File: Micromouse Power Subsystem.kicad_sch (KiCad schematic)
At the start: 3 parts, among them J2 Conn_02x16_Odd_Even, U1 INA219AxD

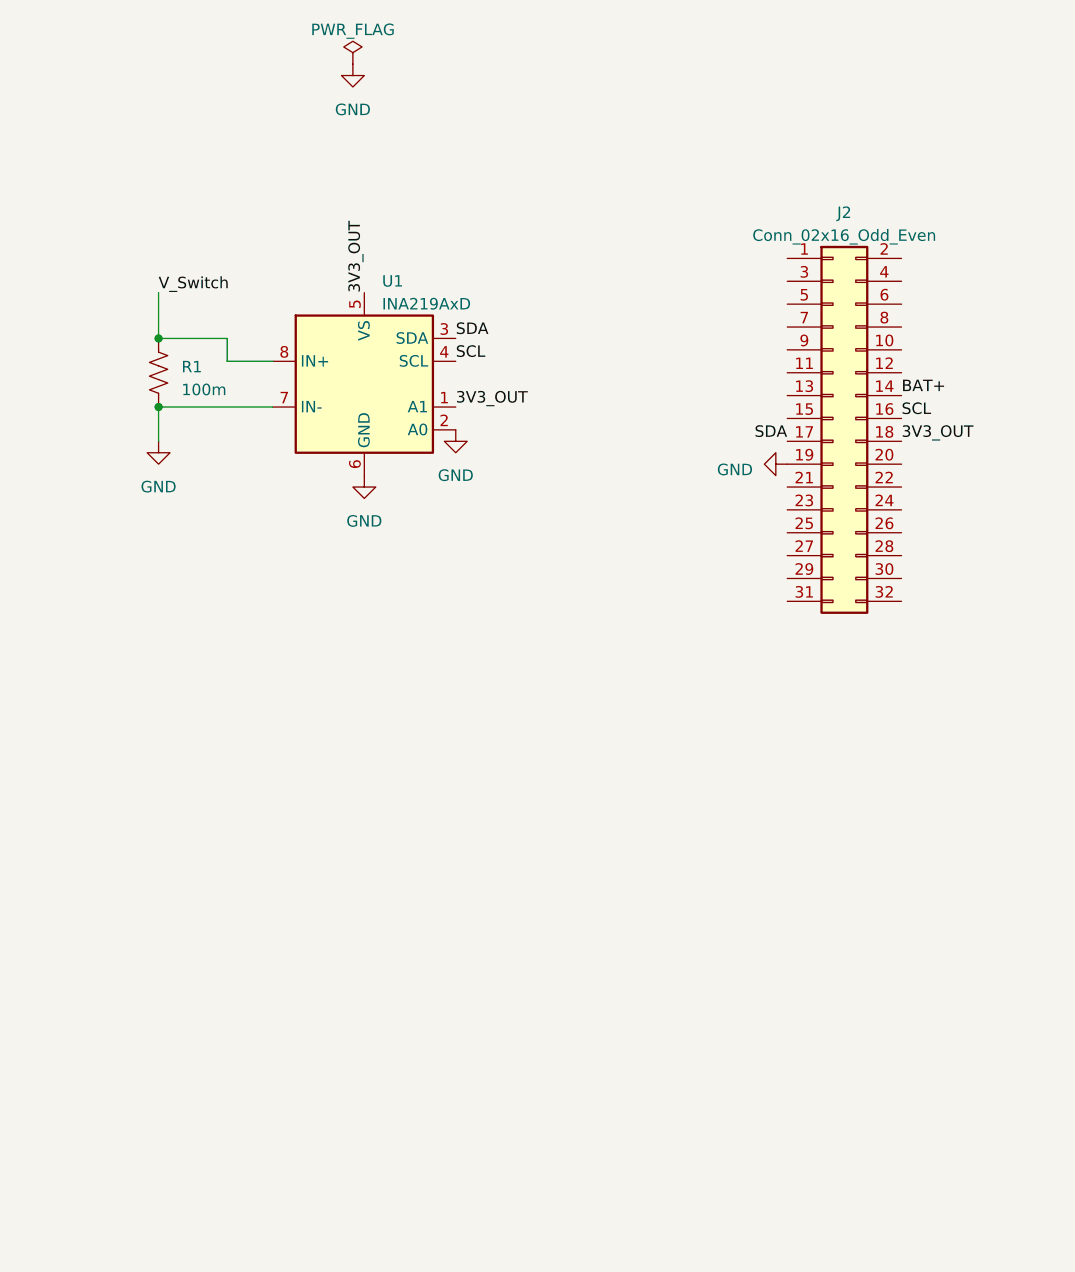
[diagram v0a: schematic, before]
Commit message: Kiyuran Task 1 Schematic Implementation Done: Added 2x external load switches with SI2301 (P-MOSFET) and 2N3904 (NPN Transistor)
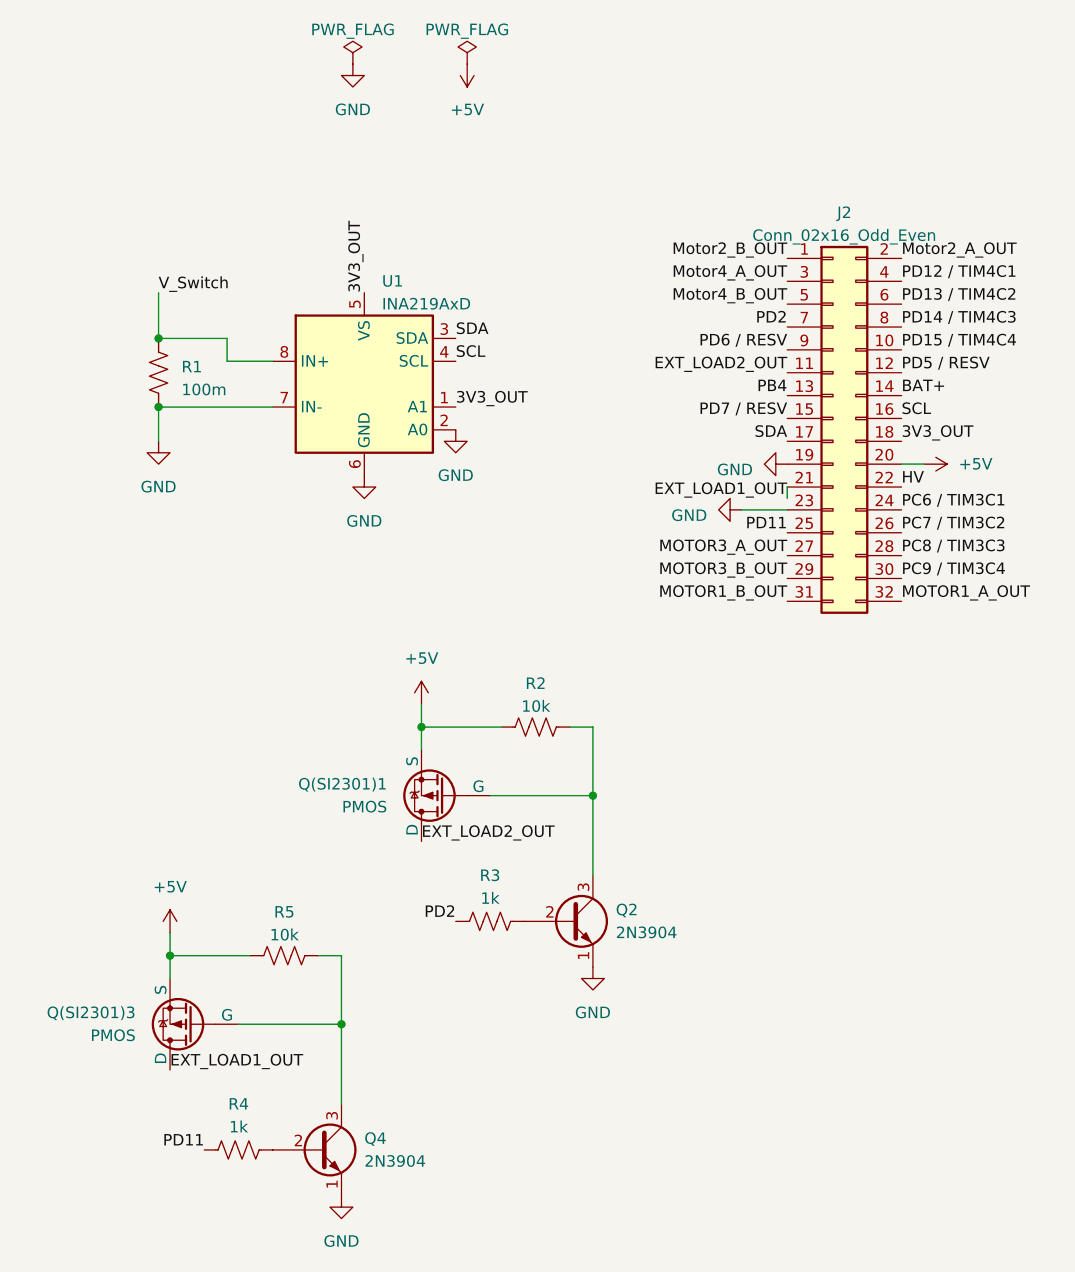
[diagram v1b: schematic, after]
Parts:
- added Q(SI2301)1, Q(SI2301)3: PMOS, symbol Simulation_SPICE:PMOS
- added Q2, Q4: 2N3904, Package_TO_SOT_THT:TO-92_Inline, symbol Transistor_BJT:2N3904
- added R2, R5: 10k, symbol Device:R_US
- added R3, R4: 1k, symbol Device:R_US
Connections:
- net GND: now also J2.23 (Pin_23), Q2.1 (E), Q4.1 (E)
- net Motor2_B_OUT: now reaches J2.1 (Pin_1)
- net PD15 / TIM4C4: now reaches J2.10 (Pin_10)
- net EXT_LOAD2_OUT: now reaches J2.11 (Pin_11)
- net EXT_LOAD2_OUT: now also Q(SI2301)1.1 (D)
- net PD5 / RESV: now reaches J2.12 (Pin_12)
- net PB4: now reaches J2.13 (Pin_13)
- net PD7 / RESV: now reaches J2.15 (Pin_15)
- net Motor2_A_OUT: now reaches J2.2 (Pin_2)
- net +5V: now reaches J2.20 (Pin_20)
- net +5V: now also Q(SI2301)1.3 (S), Q(SI2301)3.3 (S), R2.1, R5.1
- net EXT_LOAD1_OUT: now reaches J2.21 (Pin_21)
- net EXT_LOAD1_OUT: now also Q(SI2301)3.1 (D)
- net HV: now reaches J2.22 (Pin_22)
- net PC6 / TIM3C1: now reaches J2.24 (Pin_24)
- net PD11: now reaches J2.25 (Pin_25)
- net PD11: now also R4.1
- net PC7 / TIM3C2: now reaches J2.26 (Pin_26)
- net MOTOR3_A_OUT: now reaches J2.27 (Pin_27)
- net PC8 / TIM3C3: now reaches J2.28 (Pin_28)
- net MOTOR3_B_OUT: now reaches J2.29 (Pin_29)
- net Motor4_A_OUT: now reaches J2.3 (Pin_3)
- net PC9 / TIM3C4: now reaches J2.30 (Pin_30)
- net MOTOR1_B_OUT: now reaches J2.31 (Pin_31)
- net MOTOR1_A_OUT: now reaches J2.32 (Pin_32)
- net PD12 / TIM4C1: now reaches J2.4 (Pin_4)
- net Motor4_B_OUT: now reaches J2.5 (Pin_5)
- net PD13 / TIM4C2: now reaches J2.6 (Pin_6)
- net PD2: now reaches J2.7 (Pin_7)
- net PD2: now also R3.1
- net PD14 / TIM4C3: now reaches J2.8 (Pin_8)
- net PD6 / RESV: now reaches J2.9 (Pin_9)
- new net: Q2.2 (B), R3.2
- new net: Q(SI2301)1.2 (G), Q2.3 (C), R2.2
- new net: Q(SI2301)3.2 (G), Q4.3 (C), R5.2
- new net: Q4.2 (B), R4.2

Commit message: (K.2:) Added and updated Task 2: Added generic JST PH (Conn_01x02) for BAT+ to VM1/VM2/VM3 and GND to PGND2/PGND1/GND on both TB6612FNG's with 100uF and 0.1uF caps
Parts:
- removed Q(SI2301)3: PMOS, symbol Simulation_SPICE:PMOS
- removed Q4: 2N3904, Package_TO_SOT_THT:TO-92_Inline, symbol Transistor_BJT:2N3904
- added C1: 100µ, symbol Device:C_Small
- added C2: 0.1µ, symbol Device:C_Small
- added J1: Conn_01x02, Connector_JST:JST_PH_B2B-PH-K_1x02_P2.00mm_Vertical, symbol Connector_Generic:Conn_01x02
- added Q(SI2301)2: PMOS, symbol Simulation_SPICE:PMOS
- added Q1: 2N3904, Package_TO_SOT_THT:TO-92_Inline, symbol Transistor_BJT:2N3904
- added U2, U3: TB6612FNG, Package_SO:SSOP-24_5.3x8.2mm_P0.65mm, symbol Driver_Motor:TB6612FNG
- R1: footprint (none) -> Resistor_SMD:R_Shunt_Ohmite_LVK12
- R2: value 10k -> 1k
- R3: value 1k -> 10k
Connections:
- net 3V3_OUT: now also U2.19 (STBY), U2.20 (VCC), U3.19 (STBY), U3.20 (VCC)
- net BAT+: now also C1.1, C2.1, J1.1 (Pin_1), U2.13 (VM2), U2.14 (VM3), U2.24 (VM1), U3.13 (VM2), U3.14 (VM3), U3.24 (VM1)
- net EXT_LOAD1_OUT: now also Q(SI2301)1.1 (D)
- net EXT_LOAD2_OUT: now also Q(SI2301)2.1 (D); no longer Q(SI2301)1.1 (D)
- net GND: now also C1.2, C2.2, J1.2 (Pin_2), Q1.1 (E), U2.10 (PGND2), U2.18 (GND), U2.3 (PGND1), U2.4 (PGND1), U2.9 (PGND2), U3.10 (PGND2), U3.18 (GND), U3.3 (PGND1), U3.4 (PGND1), U3.9 (PGND2)
- net Motor2_A_OUT: now also U2.1 (AO1), U2.2 (AO1)
- net Motor2_B_OUT: now also U2.5 (AO2), U2.6 (AO2)
- net Motor4_A_OUT: now also U2.11 (BO1), U2.12 (BO1)
- net Motor4_B_OUT: now also U2.7 (BO2), U2.8 (BO2)
- net at R3.2: now also Q(SI2301)1.2 (G), Q1.3 (C); no longer Q2.2 (B)
- net at R5.2: now also Q2.3 (C), Q(SI2301)2.2 (G)
- net at R4.2: now also Q2.2 (B)
- net +5V renamed 5V_OUT
- net 5V_OUT: now also R3.1, Q(SI2301)2.3 (S); no longer R2.1
- net MOTOR1_A_OUT renamed Motor1_A_OUT
- net Motor1_A_OUT: now also U3.11 (BO1), U3.12 (BO1)
- net MOTOR1_B_OUT renamed Motor1_B_OUT
- net Motor1_B_OUT: now also U3.7 (BO2), U3.8 (BO2)
- net MOTOR3_A_OUT renamed Motor3_A_OUT
- net Motor3_A_OUT: now also U3.1 (AO1), U3.2 (AO1)
- net MOTOR3_B_OUT renamed Motor3_B_OUT
- net Motor3_B_OUT: now also U3.5 (AO2), U3.6 (AO2)
- net PB4 renamed FAST_CHARGE_CTRL
- net PC6 / TIM3C1 renamed Motor3_CTRL1
- net Motor3_CTRL1: now also U3.23 (PWMA)
- net PC7 / TIM3C2 renamed Motor3_CTRL2
- net Motor3_CTRL2: now also U3.21 (AIN1), U3.22 (AIN2)
- net PC8 / TIM3C3 renamed MotorR1_CTRL1
- net PC9 / TIM3C4 renamed Motor1_CTRL2
- net Motor1_CTRL2: now also U3.16 (BIN2), U3.17 (BIN1)
- net PD11 renamed CTRL_EXT_LOAD1
- net CTRL_EXT_LOAD1: now also R2.1; no longer R4.1
- net PD12 / TIM4C1 renamed Motor2_CTRL1
- net Motor2_CTRL1: now also U2.23 (PWMA)
- net PD13 / TIM4C2 renamed Motor2_CTRL2
- net Motor2_CTRL2: now also U2.21 (AIN1), U2.22 (AIN2)
- net PD14 / TIM4C3 renamed Motor4_CTRL1
- net Motor4_CTRL1: now also U2.15 (PWMB)
- net PD15 / TIM4C4 renamed Motor4_CTRL2
- net Motor4_CTRL2: now also U2.16 (BIN2), U2.17 (BIN1)
- net PD2 renamed CTRL_EXT_LOAD2
- net CTRL_EXT_LOAD2: now also R4.1; no longer R3.1
- net PD5 / RESV renamed USART2_TX
- net PD6 / RESV renamed USART2_RX
- net PD7 / RESV: no longer names the net of J2.15 (Pin_15)
- new net: Q1.2 (B), R2.2
- new net Motor1_CTRL1: U3.15 (PWMB)
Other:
- note added: "(K:) Provide 2x External Load Switching at 1A each (High Side connected to 5V)"
- moved on the sheet: J2, R1, U1

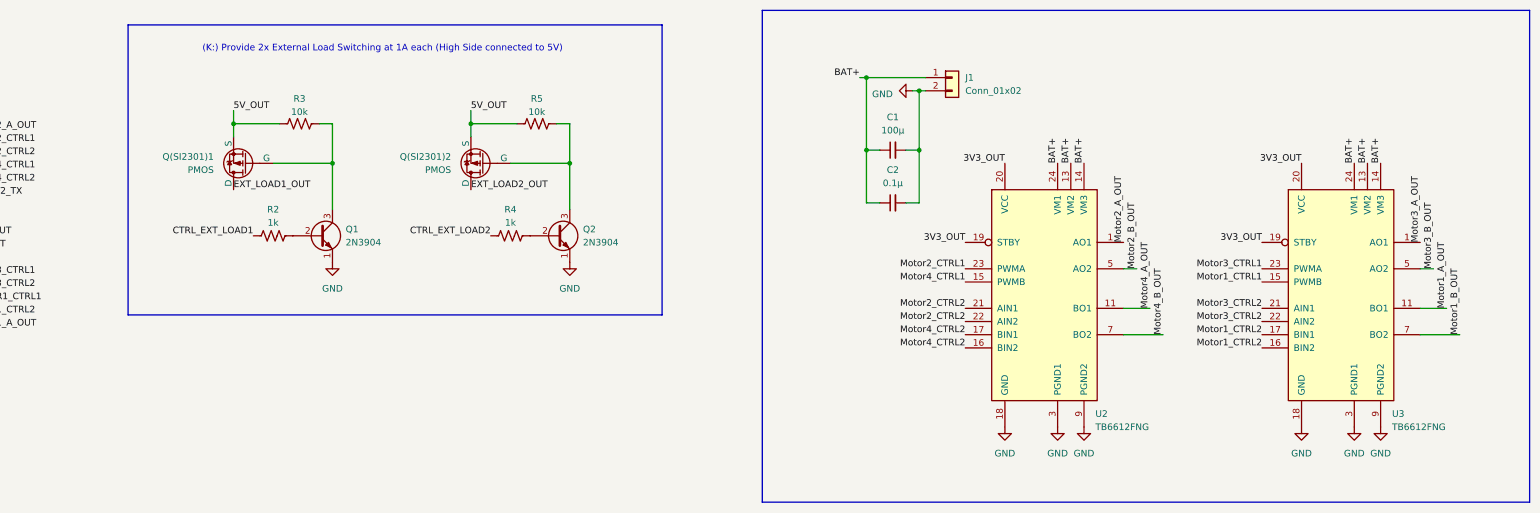
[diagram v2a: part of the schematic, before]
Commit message: (K.2:) Task 2: Used JST1/JST2 net labels at BAT+ and GND on pin 1 and 2 of J1 for clarity and to distinguish from the 2x16 header connections
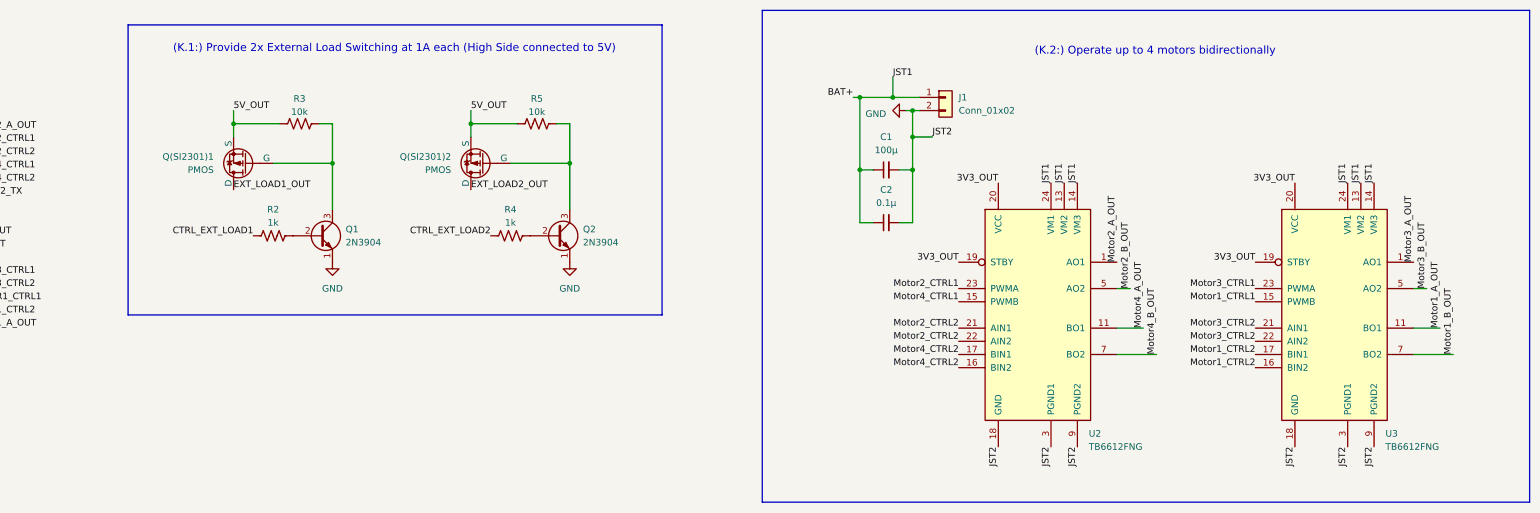
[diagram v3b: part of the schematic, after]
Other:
- note added: "(K.1:) Provide 2x External Load Switching at 1A each (High Side connected to 5V)"
- note added: "(K.2:) Operate up to 4 motors bidirectionally"
- note removed: "(K:) Provide 2x External Load Switching at 1A each (High Side connected to 5V)"
- moved on the sheet: C1, C2, J1, U2, U3

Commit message: (K.3:) Task 3: TPS61088RHLR (5V boost) and RT8059GJ5 (3.3V buck) connected with full pinout to satisfy the specifications
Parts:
- added C10, C5, C6: 10µ, symbol Device:C_Small
- added C3, C4, C9: 22µ, symbol Device:C_Small
- added C7: 1µ, symbol Device:C_Small
- added C8: 0.1µ, symbol Device:C_Small
- added L1: 2.2µ, symbol Device:L
- added L2: 4.7µ, symbol Device:L
- added Q(SI2301)3: PMOS, symbol Simulation_SPICE:PMOS
- added Q3: 2N7002, Package_TO_SOT_SMD:SOT-23, symbol Transistor_FET:2N7002
- added R10: 510k, Resistor_SMD:R_Shunt_Ohmite_LVK12, symbol Device:R_US
- added R11, R12, R6, R8: 100k, Resistor_SMD:R_Shunt_Ohmite_LVK12, symbol Device:R_US
- added R13: 10k, Resistor_SMD:R_Shunt_Ohmite_LVK12, symbol Device:R_US
- added R14: 1M, Resistor_SMD:R_Shunt_Ohmite_LVK12, symbol Device:R_US
- added R7: 19k, Resistor_SMD:R_Shunt_Ohmite_LVK12, symbol Device:R_US
- added R9: 22k, Resistor_SMD:R_Shunt_Ohmite_LVK12, symbol Device:R_US
- added SW1: ~, TS-1101S-C-B-B-B-A:SW-SMD_L6.0-W3.5-LS8.0, symbol TS-1101S-C-B-B-B-A:TS-1101S-C-B-B-B-A
- added U4: SI2301CDS-T1-GE3, TO-236_VIS, symbol 2025-03-26_09-12-34:SI2301CDS-T1-GE3
- added U5: TPS61088RHLR, TPS61088RHLR:IC_TPS61088RHLR, symbol TPS61088RHLR:TPS61088RHLR
- added U6: RT8059GJ5, TSOT-23-5_RIT, symbol 2025-03-25_16-49-52:RT8059GJ5
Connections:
- net 3V3_OUT: now also C10.2, C3.1, C5.1, C6.1, C9.2, L2.2, Q(SI2301)3.1 (D), R8.1, U5.2 (EN), U5.9 (VIN), U6.4 (VIN)
- net 5V_OUT: now also C4.1, L1.1, R6.2, U5.14 (VOUT_16), U5.15 (VOUT_14), U5.16 (VOUT_15)
- net BAT+: now also Q(SI2301)3.3 (S), R14.1, U6.1 (EN)
- net GND: now also C10.1, C3.2, C4.2, C5.2, C6.2, C7.2, C9.1, Q3.2 (S), R11.1, R12.2, R7.2, R9.1, U5.11 (NC_11), U5.12 (NC_12), U5.20 (AGND), U5.21 (PGND), U5.22 (PGND), U5.23 (PGND), U5.24 (PGND), U5.25 (PGND), U5.26 (PGND), U5.27 (PGND), U5.28 (PGND), U5.29 (PGND), U6.2 (GND)
- new net: Q(SI2301)3.2 (G), Q3.3 (D), R13.2
- new net: C7.1, U5.1 (VCC)
- new net: Q3.1 (G), R12.1, SW1.2
- new net: R6.1, R7.1, U5.17 (FB)
- new net: R14.2, SW1.1
- new net: R10.1, U5.3 (FSW)
- new net: R8.2, R9.2, U6.5 (FB)
- new net: C8.1, U5.8 (BOOT)
- new net: R11.2, U5.19 (ILIM)
- new net: L2.1, U6.3 (LLX)
- new net SW: C8.2, L1.2, R10.2, U5.4 (SW_7), U5.5 (SW_4), U5.6 (SW_5), U5.7 (SW_6)
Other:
- note added: "(K.3:) Provide an ON/OFF switch. OFF state: battery draw <30uA. ON state: can provide your robot peak current of 2A. The switch needs to shut down 5V and 3V3."

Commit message: (K.4:) Task 4: Implemented ON/OFF with SI2301CDS-T1-GE3 P-MOSFET and K3-1296S-E1 slide switch, and finalised the schematic designs of the other tasks
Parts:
- removed Q3: 2N7002, Package_TO_SOT_SMD:SOT-23, symbol Transistor_FET:2N7002
- removed R13: 10k, Resistor_SMD:R_Shunt_Ohmite_LVK12, symbol Device:R_US
- removed R14: 1M, Resistor_SMD:R_Shunt_Ohmite_LVK12, symbol Device:R_US
- removed SW1: ~, TS-1101S-C-B-B-B-A:SW-SMD_L6.0-W3.5-LS8.0, symbol TS-1101S-C-B-B-B-A:TS-1101S-C-B-B-B-A
- removed U4: SI2301CDS-T1-GE3, TO-236_VIS, symbol 2025-03-26_09-12-34:SI2301CDS-T1-GE3
- added C11: 10n, symbol Device:C_Small
- added SW1: ~, K3-1296S-E1_C128955:SW-TH_K3-1296S-E1, symbol K3-1296S-E1_C128955:K3-1296S-E1_C128955
- R12: value 100k -> 10k
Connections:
- net 3V3_OUT: now also J1.1 (Pin_1), J2.14 (Pin_14), Q(SI2301)3.3 (S), R12.2; no longer C10.2, C3.1, C9.2, Q(SI2301)3.1 (D), U5.2 (EN), U5.9 (VIN)
- net FAST_CHARGE_CTRL: now also U3.16 (BIN2)
- net GND: now also C1.1, C11.1, SW1.1; no longer C1.2, R12.2, U5.11 (NC_11), U5.12 (NC_12)
- net Motor1_CTRL2: no longer U3.16 (BIN2)
- net Motor2_CTRL2: no longer U2.22 (AIN2)
- net Motor3_CTRL2: no longer U3.22 (AIN2)
- net Motor4_CTRL2: no longer U2.16 (BIN2)
- net USART2_RX: now also U2.22 (AIN2)
- net USART2_TX: now also U2.16 (BIN2)
- net at Q(SI2301)3.2 (G): now also R12.1, SW1.2
- net at U5.10 (SS): now also C11.2
- net VIN_SWITCHED: now reaches U5.13 (MODE)
- net VIN_SWITCHED: now also C1.2, C10.2, C2.1, C3.1, C9.2, Q(SI2301)3.1 (D), U2.13 (VM2), U2.14 (VM3), U2.24 (VM1), U3.13 (VM2), U3.14 (VM3), U3.24 (VM1), U5.2 (EN), U5.9 (VIN), U6.1 (EN)
- net PD7/RESV: now reaches J2.15 (Pin_15)
- net PD7/RESV: now also U3.22 (AIN2)
- removed net BAT+: C1.1, C2.1, J1.1 (Pin_1), J2.14 (Pin_14), Q(SI2301)3.3 (S), U2.13 (VM2), U2.14 (VM3), U2.24 (VM1), U3.13 (VM2), U3.14 (VM3), U3.24 (VM1), U6.1 (EN)
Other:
- note added: "(K.4:) Provide an ON/OFF switch"
- moved on the sheet: C10, C9, J1, L1, U3
